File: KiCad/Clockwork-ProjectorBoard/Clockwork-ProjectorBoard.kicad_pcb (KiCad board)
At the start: 2 copper layers, 54.4 x 23.5 mm, 31 parts, among them J1 to TCA955 PCB, J2 to DIN connecting 3+1 Socket 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, J3 to Lamp Relay Board, J4 to DIN Socket traces, J5 Relais Board, J6 uC Cable, Q1 AO3400A, U1 AP63205WU, U3 TS5A3160DBVR-TP, U4 TS5A3160DBVR-TP, U5 TSV911ILT

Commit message: Renaming once more
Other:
- board text added: "Clockwork Projector Board for Bauer T610 / T525"
- board text removed: "SynCrystal Projector Board for Bauer T610 / T525"
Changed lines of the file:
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@@
 		(layer "Edge.Cuts")
 	)
-	(gr_text "SynCrystal Projector Board for Bauer T610 / T525"
+	(gr_text "Clockwork Projector Board for Bauer T610 / T525"
 		(at 172.085 91.44 0)
 		(layer "B.SilkS")

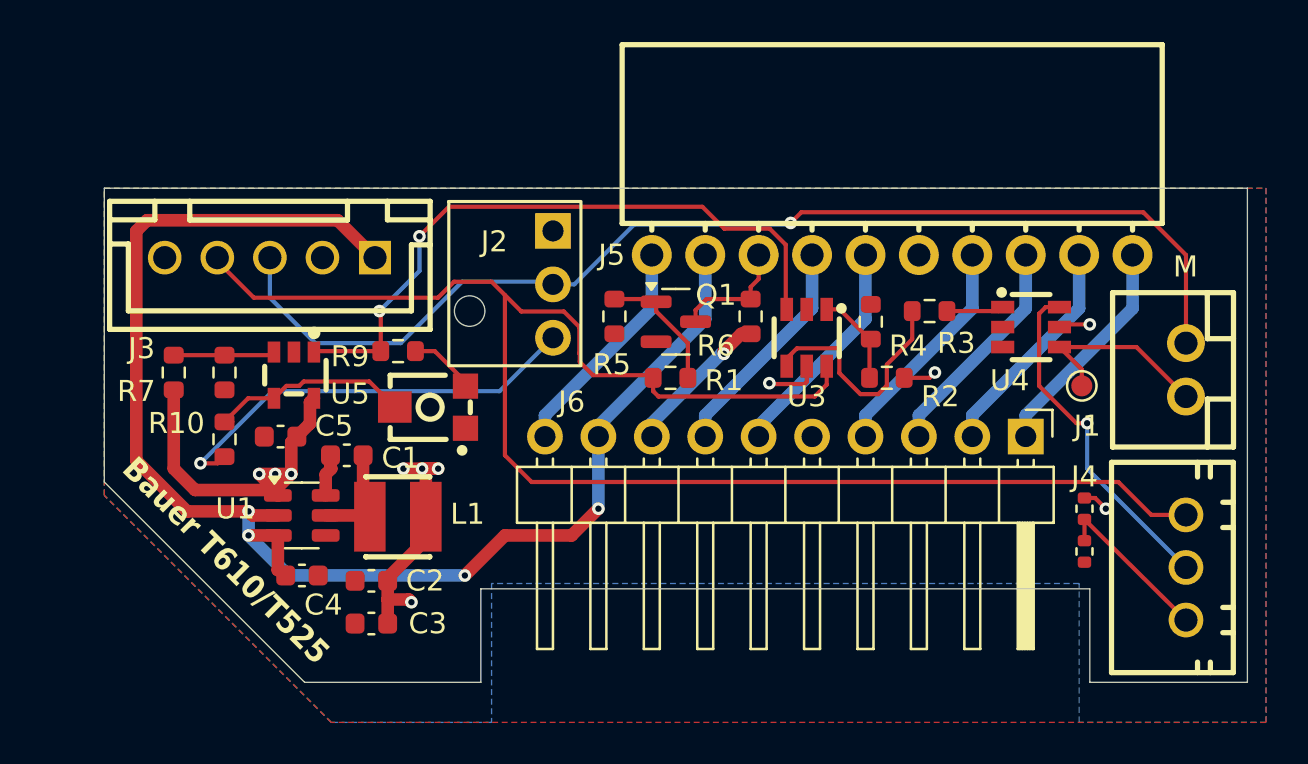
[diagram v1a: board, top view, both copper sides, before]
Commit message: New Gerbers, added the xtal to the BOM, new MH for OLED
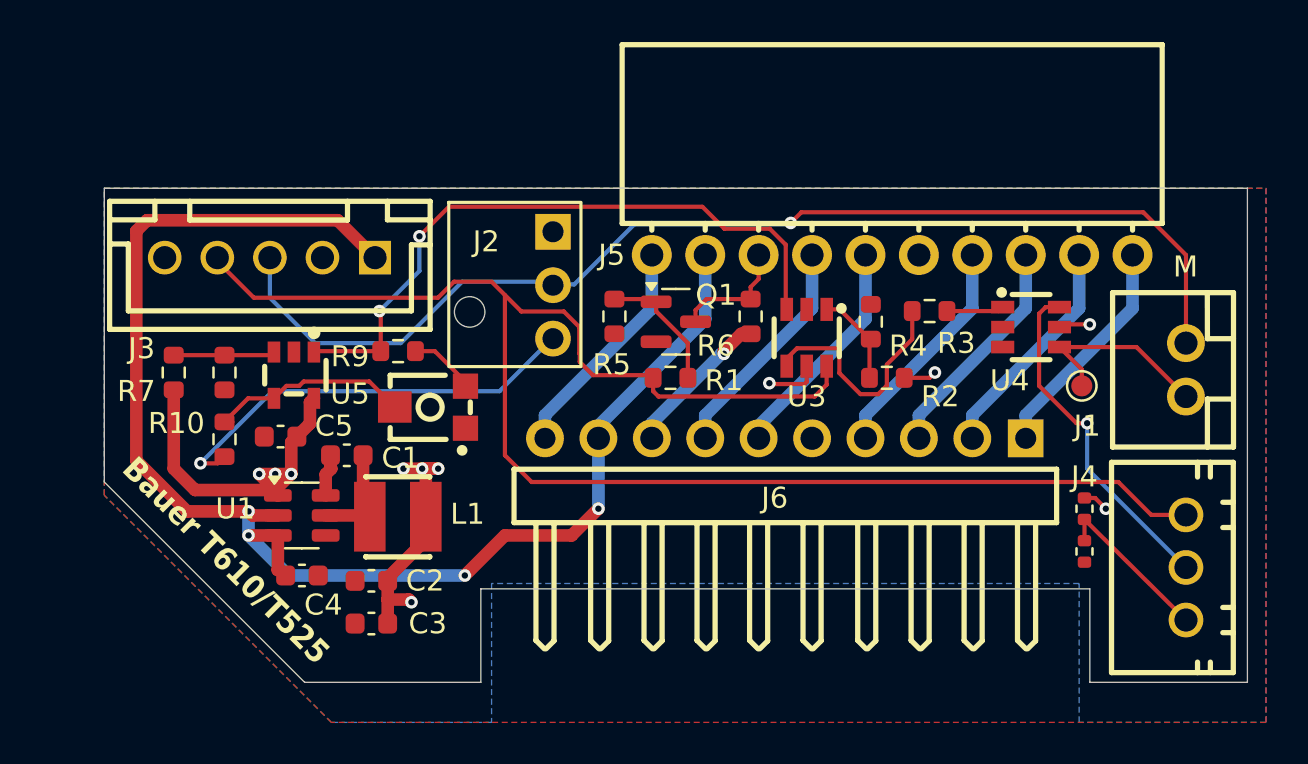
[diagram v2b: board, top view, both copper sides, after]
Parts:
- J6: footprint Connector_PinHeader_2.54mm:PinHeader_1x10_P2.54mm_Horizontal -> easyEDA:HDR-TH_10P-P2.54-H-M-W10.4_flipped
- RV1: value 300 -> 500
- moved J6 11.4 mm to (195.6, 88.1), turned to 0 degrees
- moved J2 2.54 mm to (184.5, 80.8)

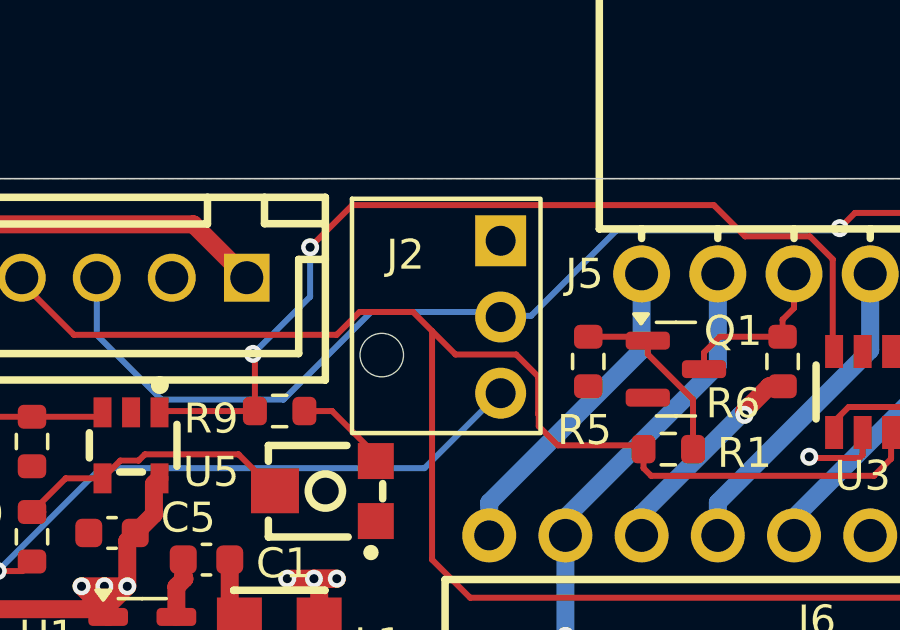
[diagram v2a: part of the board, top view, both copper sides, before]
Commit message: Starting Rev.B, fixing DIN-Connector-Wire Pin 2/3 to keep DIN/JST pin alignment
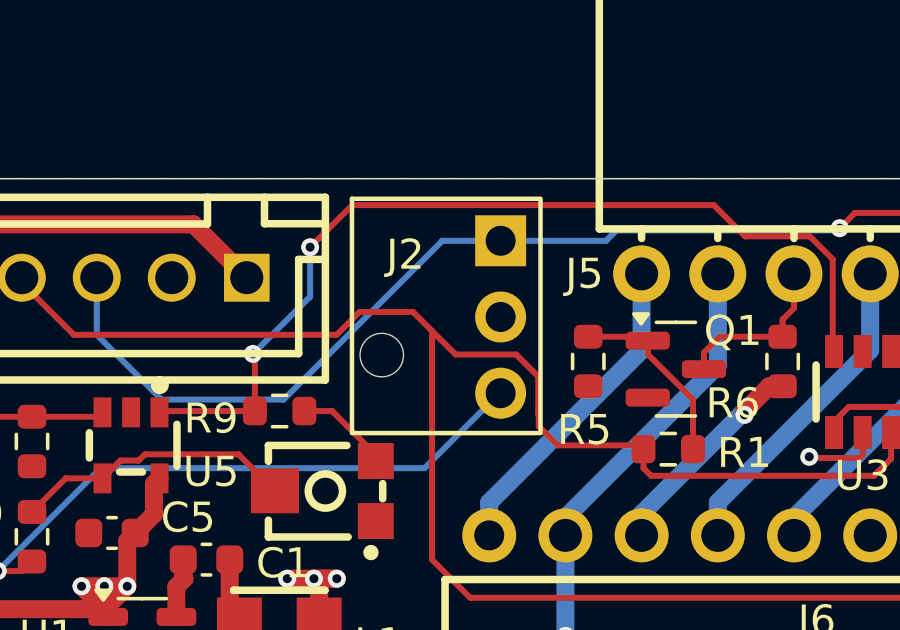
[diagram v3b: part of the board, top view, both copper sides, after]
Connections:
- J2 pad 1: +5V -> /M-Pin
- J2 pad 2: /M-Pin -> +5V
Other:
- board text added: "Rev.B"
- board text removed: "Rev.A"
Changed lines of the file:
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@@
 			(layers "*.Cu" "*.Mask")
 			(remove_unused_layers no)
-			(net 4 "+5V")
+			(net 6 "/M-Pin")
 			(pinfunction "Pin_1")
 			(pintype "passive")
@@
 			(layers "*.Cu" "*.Mask")
 			(remove_unused_layers no)
-			(net 6 "/M-Pin")
+			(net 4 "+5V")
 			(pinfunction "Pin_2")
 			(pintype "passive")
@@
 		)
 	)
-	(gr_text "Rev.A"
+	(gr_text "Rev.B"
 		(at 180.34 98.552 0)
 		(layer "B.SilkS")
@@
 	)
 	(segment
+		(start 184.404 80.645)
+		(end 184.531 80.772)
+		(width 0.2)
+		(layer "B.Cu")
+		(net 4)
+	)
+	(segment
 		(start 182.245 92.71)
 		(end 180.34 94.615)
@@
 	)
 	(segment
-		(start 180.213 80.645)
-		(end 184.404 80.645)
+		(start 188.394 77.925)
+		(end 188.047 78.272)
 		(width 0.2)
 		(layer "B.Cu")
@@
 	)
 	(segment
-		(start 171.069 81.407)
-		(end 173.228 83.566)
+		(start 188.047 78.272)
+		(end 184.531 78.272)
 		(width 0.2)
 		(layer "B.Cu")
@@
 	)
 	(segment
-		(start 173.228 83.566)
-		(end 177.292 83.566)
-		(width 0.2)
-		(layer "B.Cu")
-		(net 6)
-	)
-	(segment
-		(start 171.069 79.502)
-		(end 171.069 81.407)
+		(start 171.069 81.407)
+		(end 173.228 83.566)
 		(width 0.2)
 		(layer "B.Cu")
@@
 	(segment
 		(start 177.292 83.566)
-		(end 180.213 80.645)
+		(end 182.586 78.272)
 		(width 0.2)
 		(layer "B.Cu")
@@
 	)
 	(segment
-		(start 184.404 80.645)
-		(end 184.531 80.772)
+		(start 182.586 78.272)
+		(end 184.531 78.272)
 		(width 0.2)
 		(layer "B.Cu")
@@
 	)
 	(segment
-		(start 188.394 77.925)
-		(end 185.547 80.772)
+		(start 173.228 83.566)
+		(end 177.292 83.566)
 		(width 0.2)
 		(layer "B.Cu")
@@
 	)
 	(segment
-		(start 185.547 80.772)
-		(end 184.531 80.772)
+		(start 195.76 77.925)
+		(end 188.394 77.925)
 		(width 0.2)
 		(layer "B.Cu")
@@
 	)
 	(segment
-		(start 195.76 77.925)
-		(end 188.394 77.925)
+		(start 171.069 79.502)
+		(end 171.069 81.407)
 		(width 0.2)
 		(layer "B.Cu")

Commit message: Fixes the Voltage Divider for the STOP Voltage, which turned out too low
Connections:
- net Net-(J4-Pin_3) renamed /Proj_ID
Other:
- board text added: "1"
- board text added: "5"
- board text added: "6"
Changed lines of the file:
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@@
 	(net 28 "Net-(R9-Pad1)")
 	(net 29 "Net-(U5--)")
-	(net 30 "Net-(J4-Pin_3)")
+	(net 30 "/Proj_ID")
 	(footprint "TestPoint:TestPoint_Pad_D1.0mm"
 		(layer "F.Cu")
@@
 			(layers "F.Cu" "F.Paste" "F.Mask")
 			(roundrect_rratio 0.25)
-			(net 30 "Net-(J4-Pin_3)")
+			(net 30 "/Proj_ID")
 			(pintype "passive")
 		)
@@
 			(layers "F.Cu" "F.Paste" "F.Mask")
 			(roundrect_rratio 0.25)
-			(net 30 "Net-(J4-Pin_3)")
+			(net 30 "/Proj_ID")
 			(pintype "passive")
 		)
@@
 			(layers "*.Cu" "*.Mask")
 			(remove_unused_layers no)
-			(net 30 "Net-(J4-Pin_3)")
+			(net 30 "/Proj_ID")
 			(pinfunction "Pin_3")
 			(pintype "passive")
@@
 		(layer "Edge.Cuts")
 	)
+	(gr_text "1"
+		(at 216.7 92.1 0)
+		(layer "B.SilkS")
+		(effects
+			(font
+				(size 1 1)
+				(thickness 0.1)
+			)
+			(justify left bottom mirror)
+		)
+	)
 	(gr_text "Clockwork Projector Board for Bauer T610 / T525"
 		(at 172.085 91.44 0)
@@
 			)
 			(justify left bottom mirror)
+		)
+	)
+	(gr_text "6"
+		(at 216.7 97.3 0)
+		(layer "B.SilkS")
+		(effects
+			(font
+				(size 1 1)
+				(thickness 0.1)
+			)
+			(justify left bottom mirror)
+		)
+	)
+	(gr_text "5"
+		(at 216.7 94.8 0)
+		(layer "B.SilkS")
+		(effects
+			(font
+				(size 1 1)
+				(thickness 0.1)
+			)
+			(justify left bottom mirror)

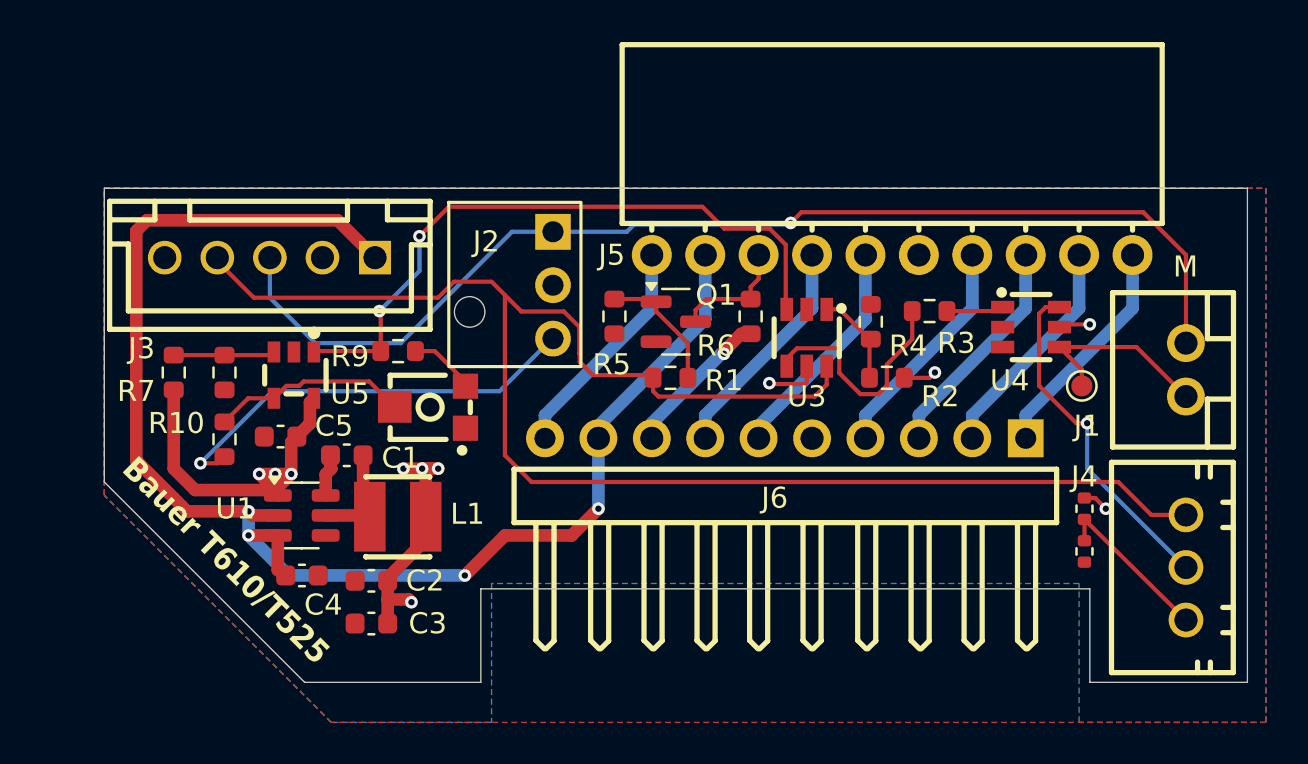
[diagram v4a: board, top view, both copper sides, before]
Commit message: Adding a 6th Pin to the Lamp Relais Connector, which pulls the MOSFET high, disabling the built-in Relay
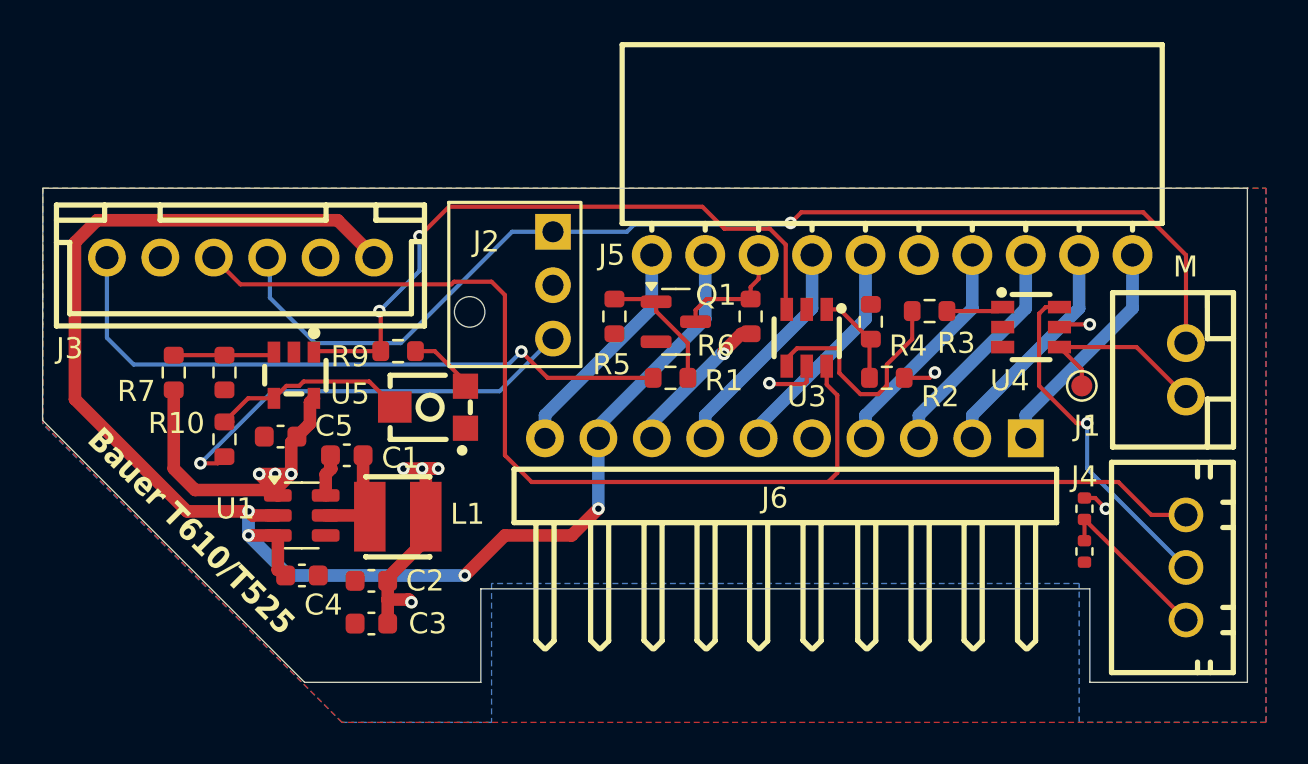
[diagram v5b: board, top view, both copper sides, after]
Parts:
- J3: footprint easyEDA:CONN-TH_5P-P2.50_ZX-XH2.54-5PZZ -> easyEDA:CONN-TH_6P-P2.54_ZX-XH2.54-6PZZ-R
- R2: value 6k8 -> 3k3
- R4: value 2k7 -> 4k3
- moved J3 1.40 mm to (169.7, 79.5), turned to 0 degrees
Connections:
- R1 pad 1: /Stop_EN -> /Overwrite_Relais
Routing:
- net /Overwrite_Relais: track 0.00 -> 31.3 mm, vias 0 -> 1
- net /Stop_EN: track 76.3 -> 61.9 mm
- net +15V: track 68.1 -> 71.9 mm
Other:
- board size 54.4 x 23.5 mm -> 57.3 x 23.5 mm
- board text added: "678"

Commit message: Optimize Projector Board Size, red socket will fit better.
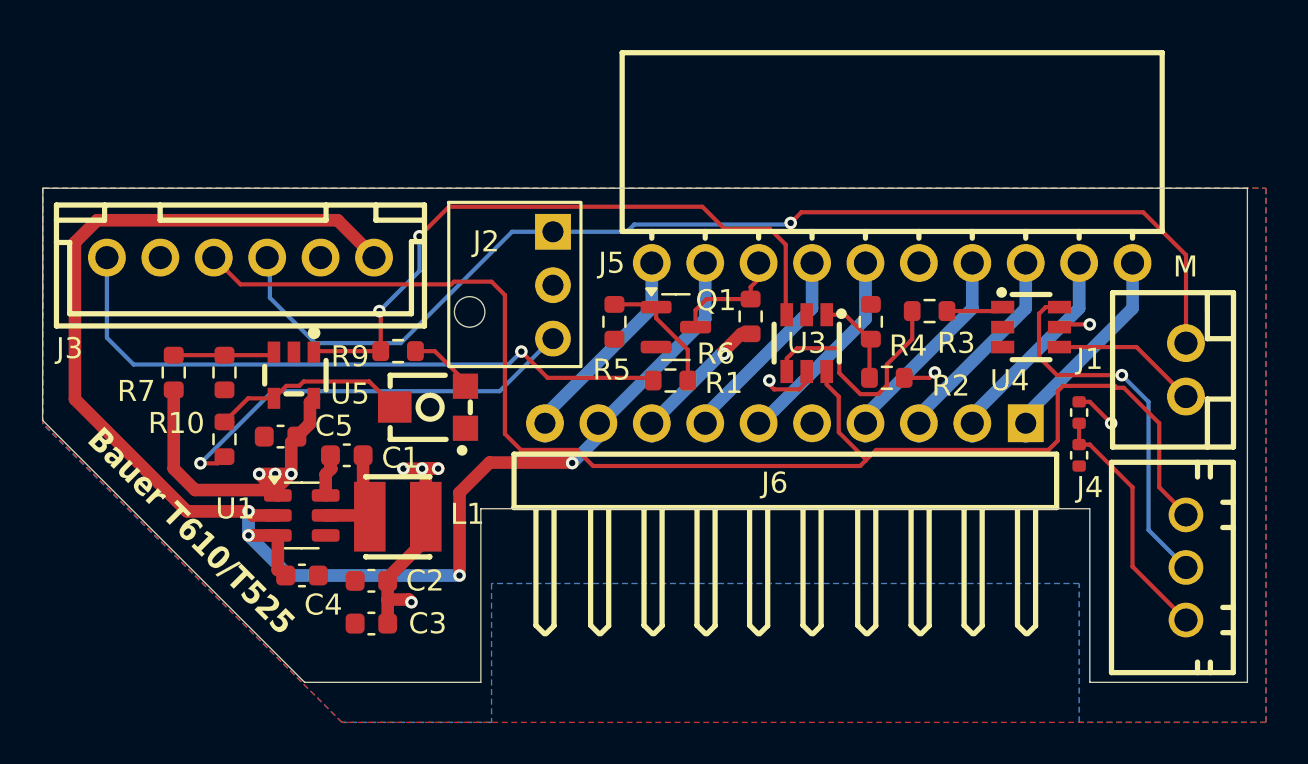
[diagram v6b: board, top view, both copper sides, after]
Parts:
- removed TP1: 678, TestPoint:TestPoint_Pad_D1.0mm
- moved R12 4.58 mm to (209.6, 86.9)
- moved R11 4.58 mm to (209.6, 88.9)
- moved J6 0.72 mm to (195.6, 87.4)
- moved J5 0.38 mm to (200.7, 79.8)
- moved Q1 0.25 mm to (190.4, 82.8)
- moved U3 0.25 mm to (196.6, 83.6)
- moved R5 0.25 mm to (187.5, 82.5)
- moved R1 0.13 mm to (190.1, 85.3)
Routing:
- net /Stop_EN: track 61.9 -> 66.7 mm
- net /Proj_ID: track 7.81 -> 11.8 mm
- net /Pin_678: track 9.27 -> 6.99 mm
- net /DAC_EN: track 16.4 -> 17.9 mm
- net +5V: track 36.3 -> 37.2 mm
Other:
- outline, holes or cut-outs redrawn
